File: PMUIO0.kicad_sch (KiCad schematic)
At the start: 3 parts, among them J1 Micro_SD_Card_Det1, U1 rv1126/rv1109

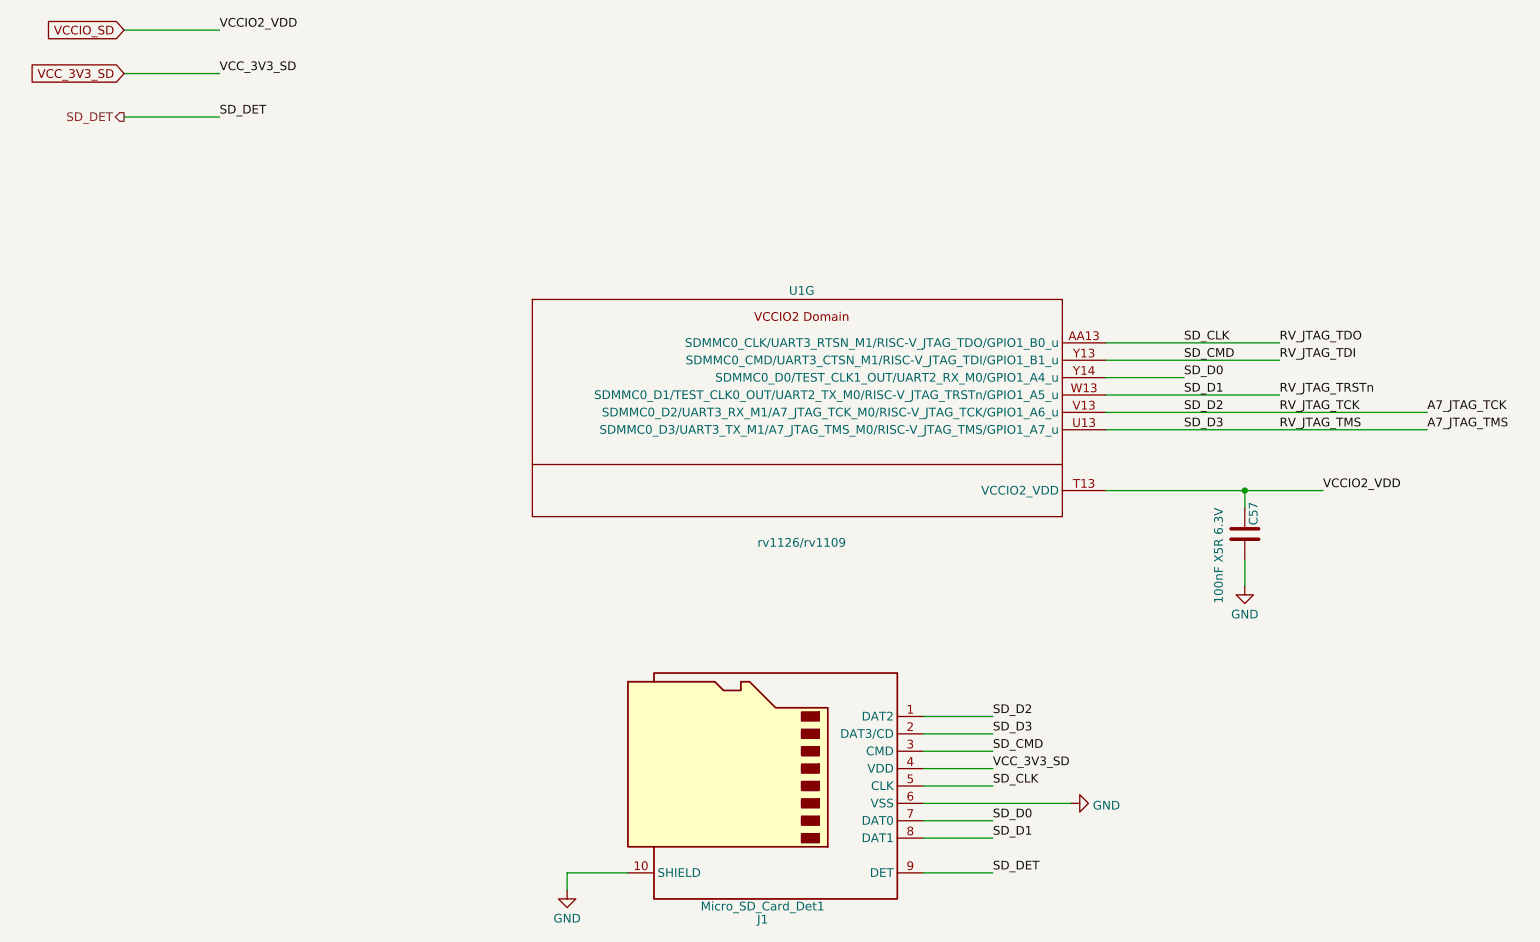
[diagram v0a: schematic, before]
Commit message: added MicroSD
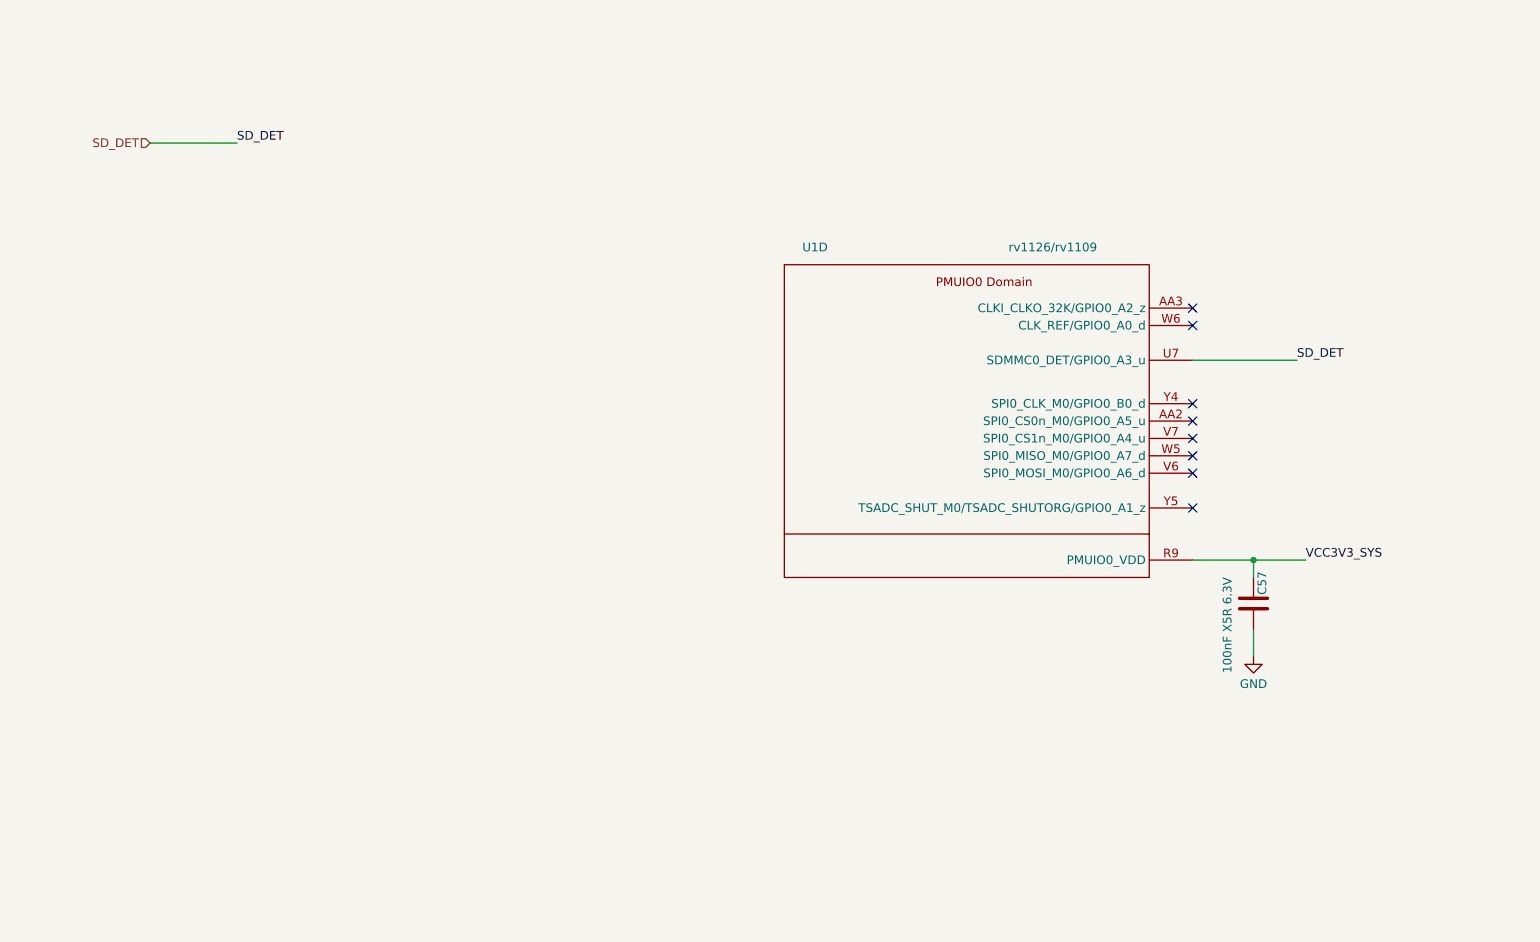
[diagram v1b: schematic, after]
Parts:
- removed J1: Micro_SD_Card_Det1, symbol Connector:Micro_SD_Card_Det1
- removed U1: rv1126/rv1109, symbol CPU_Rockchip:rv1126_rv1109
- added U1: rv1126/rv1109, symbol CPU_Rockchip:rv1126_rv1109
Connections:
- net SD_DET: now also U1.U7 (SDMMC0_DET/GPIO0_A3_u)
- net VCCIO_SD renamed VCC3V3_SYS
- net VCC3V3_SYS: now also U1.R9 (PMUIO0_VDD)
- no-connect marks 0 -> 8
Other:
- company: Qingdao IotPi Information Technology -> (none)
- title: Leaf RV1126 RK809 SDCard -> (none)

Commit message: updated footprints
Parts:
- U1: footprint (none) -> Rockchip_SoC:Rockchip_RV1126_FCCSP409LD_14.0x14.0mm
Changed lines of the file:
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@@
         )
         (path "/e3b58043-16a3-43c8-9fad-9c9784eebfa4/37e5f808-83b1-4839-b7a1-9684da8ab3e5"
-          (reference "#PWR076") (unit 1)
+          (reference "#PWR0127") (unit 1)
         )
       )
@@
       (effects (font (size 1.27 1.27)) (justify right))
     )
-    (property "Footprint" "" (at 180.34 104.14 0)
+    (property "Footprint" "Rockchip_SoC:Rockchip_RV1126_FCCSP409LD_14.0x14.0mm" (at 180.34 104.14 0)
       (effects (font (size 1.27 1.27)) hide)
     )
@@
         )
         (path "/e3b58043-16a3-43c8-9fad-9c9784eebfa4/37e5f808-83b1-4839-b7a1-9684da8ab3e5"
-          (reference "C101") (unit 1)
+          (reference "C139") (unit 1)
         )
       )

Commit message: updated Capacitors
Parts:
- C57: LCSC (none) -> C76934; Model (none) -> GRM033R61A104KE15D; Vendor (none) -> muRata(村田)
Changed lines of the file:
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@@
+      (effects (font (size 1.27 1.27)) hide)
+    )
+    (property "Description" "容值: 100nF 精度: ±10% 额定电压: 10V 材质(温度系数): X5R 材质:X5R" (at 195.58 105.41 0)
+      (effects (font (size 1.27 1.27)) hide)
+    )
+    (property "LCSC" "C76934" (at 195.58 105.41 0)
+      (effects (font (size 1.27 1.27)) hide)
+    )
+    (property "Model" "GRM033R61A104KE15D" (at 195.58 105.41 0)
+      (effects (font (size 1.27 1.27)) hide)
+    )
+    (property "Vendor" "muRata(村田)" (at 195.58 105.41 0)
       (effects (font (size 1.27 1.27)) hide)
     )

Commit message: layout SoC Power and DDR capacitors
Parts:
- C57: LCSC C76934 -> C76928; Model GRM033R61A104KE15D -> GRM033R60J104KE19D
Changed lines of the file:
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@@
       (effects (font (size 1.27 1.27)) hide)
     )
-    (property "Description" "容值: 100nF 精度: ±10% 额定电压: 10V 材质(温度系数): X5R 材质:X5R" (at 195.58 105.41 0)
+    (property "Description" "容值: 100nF 精度: ±10% 额定电压: 6.3V 材质(温度系数): X5R 材质:X5R" (at 195.58 105.41 0)
       (effects (font (size 1.27 1.27)) hide)
     )
-    (property "LCSC" "C76934" (at 195.58 105.41 0)
+    (property "LCSC" "C76928" (at 195.58 105.41 0)
       (effects (font (size 1.27 1.27)) hide)
     )
-    (property "Model" "GRM033R61A104KE15D" (at 195.58 105.41 0)
+    (property "Model" "GRM033R60J104KE19D" (at 195.58 105.41 0)
       (effects (font (size 1.27 1.27)) hide)
     )

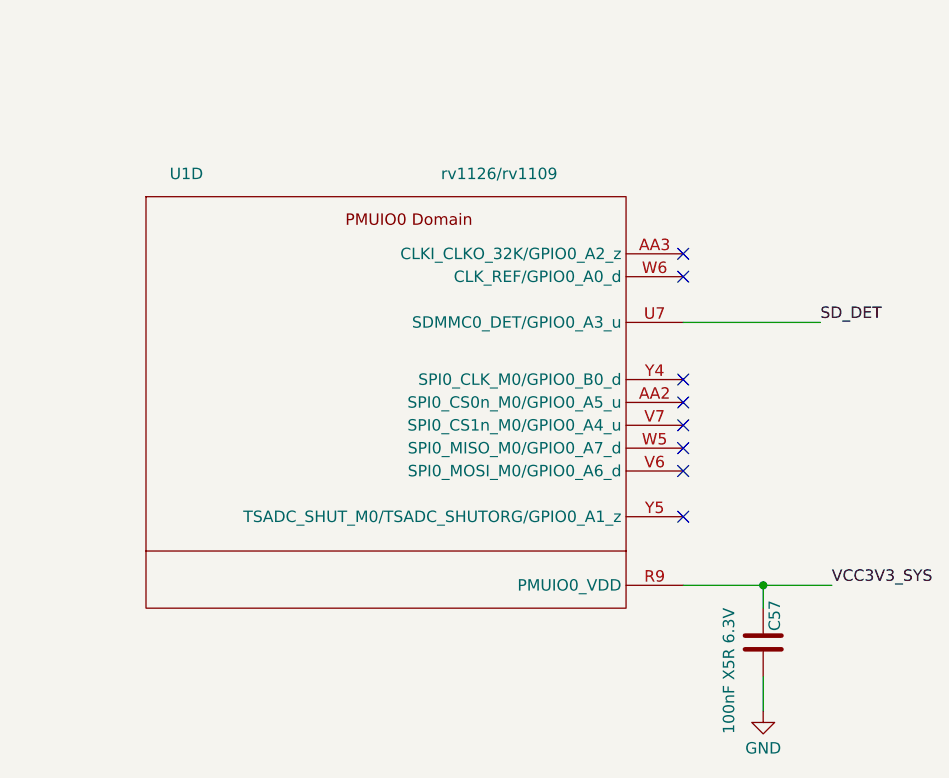
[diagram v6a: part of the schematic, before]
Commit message: fix some ERCs
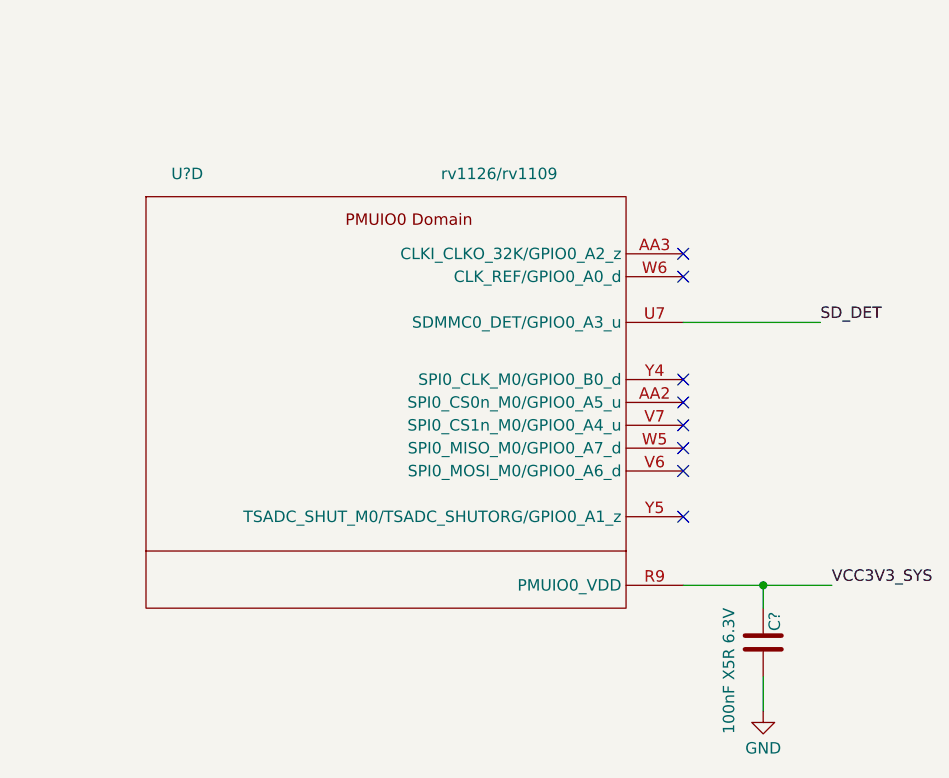
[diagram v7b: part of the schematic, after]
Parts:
- renumbered C57 to C?, U1 to U?
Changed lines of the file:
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@@
   (symbol (lib_id "power:GND") (at 195.58 113.03 0) (unit 1)
     (in_bom yes) (on_board yes) (dnp no) (fields_autoplaced)
-    (property "Reference" "#PWR074" (at 195.58 119.38 0)
+    (property "Reference" "#PWR?" (at 195.58 119.38 0)
       (effects (font (size 1.27 1.27)) hide)
     )
@@
       (project "leaf"
         (path "/e3b58043-16a3-43c8-9fad-9c9784eebfa4/4417415c-26f1-4372-988d-9fdf1c116b4b"
-          (reference "#PWR074") (unit 1)
+          (reference "#PWR?") (unit 1)
         )
         (path "/e3b58043-16a3-43c8-9fad-9c9784eebfa4/37e5f808-83b1-4839-b7a1-9684da8ab3e5"
-          (reference "#PWR0127") (unit 1)
+          (reference "#PWR0126") (unit 1)
         )
       )
@@
   (symbol (lib_id "CPU_Rockchip:rv1126_rv1109") (at 153.67 77.47 0) (unit 4)
     (in_bom yes) (on_board yes) (dnp no)
-    (property "Reference" "U1" (at 133.35 53.34 0)
+    (property "Reference" "U?" (at 133.35 53.34 0)
       (effects (font (size 1.27 1.27)) (justify right))
     )
@@
     (pin "Y21")
     (pin "C21")
-    (pin "D20")
     (pin "D21")
     (pin "E19")
@@
       (project "leaf"
         (path "/e3b58043-16a3-43c8-9fad-9c9784eebfa4/4417415c-26f1-4372-988d-9fdf1c116b4b"
-          (reference "U1") (unit 4)
+          (reference "U?") (unit 4)
         )
         (path "/e3b58043-16a3-43c8-9fad-9c9784eebfa4/37e5f808-83b1-4839-b7a1-9684da8ab3e5"
@@
   (symbol (lib_id "Device:C") (at 195.58 105.41 0) (unit 1)
     (in_bom yes) (on_board yes) (dnp no)
-    (property "Reference" "C57" (at 196.85 104.14 90)
+    (property "Reference" "C?" (at 196.85 104.14 90)
       (effects (font (size 1.27 1.27)) (justify left))
     )
@@
       (project "leaf"
         (path "/e3b58043-16a3-43c8-9fad-9c9784eebfa4/9453ad46-b3ff-4d4e-8aa6-7cc75aa0f522/f6658df5-193a-49b6-ab60-4ac3c0bbbc45"
-          (reference "C57") (unit 1)
+          (reference "C?") (unit 1)
         )
         (path "/e3b58043-16a3-43c8-9fad-9c9784eebfa4/9453ad46-b3ff-4d4e-8aa6-7cc75aa0f522/f6658df5-193a-49b6-ab60-4ac3c0bbbc45/b7d33089-b835-4c65-840f-b2075d1befa5"
-          (reference "C59") (unit 1)
+          (reference "C?") (unit 1)
         )
         (path "/e3b58043-16a3-43c8-9fad-9c9784eebfa4/9453ad46-b3ff-4d4e-8aa6-7cc75aa0f522"
-          (reference "C84") (unit 1)
+          (reference "C?") (unit 1)
         )
         (path "/e3b58043-16a3-43c8-9fad-9c9784eebfa4/cc9fb3ac-19c3-47a8-ba7d-678b4d514ff0/8aa2eca1-edfe-4e9d-a854-96f51e82fbdb"
-          (reference "C90") (unit 1)
+          (reference "C?") (unit 1)
         )
         (path "/e3b58043-16a3-43c8-9fad-9c9784eebfa4/4417415c-26f1-4372-988d-9fdf1c116b4b"
-          (reference "C100") (unit 1)
+          (reference "C?") (unit 1)
         )
         (path "/e3b58043-16a3-43c8-9fad-9c9784eebfa4/37e5f808-83b1-4839-b7a1-9684da8ab3e5"
-          (reference "C139") (unit 1)
+          (reference "C135") (unit 1)
         )
       )

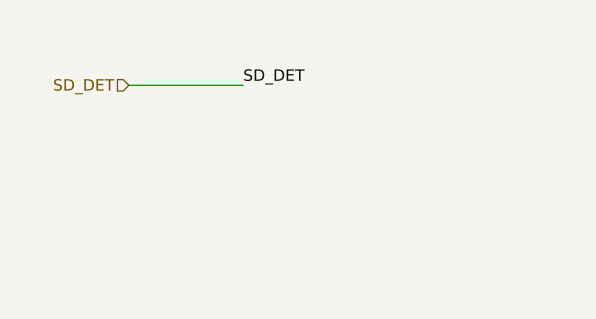
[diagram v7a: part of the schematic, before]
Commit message: fix ERC
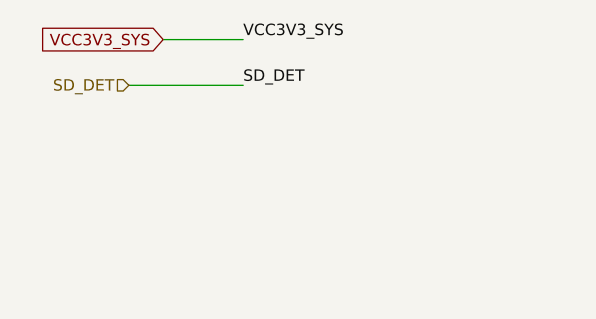
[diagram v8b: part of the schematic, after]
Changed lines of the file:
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@@
+    (stroke (width 0) (type default))
+  )
+  (wire (pts (xy 38.1 33.02) (xy 46.99 33.02))
     (stroke (width 0) (type default))
   )
@@
     (effects (font (size 1.27 1.27)) (justify left bottom))
   )
+  (label "VCC3V3_SYS" (at 46.99 33.02 0) (fields_autoplaced)
+    (effects (font (size 1.27 1.27)) (justify left bottom))
+  )
+  (global_label "VCC3V3_SYS" (shape input) (at 38.1 33.02 180) (fields_autoplaced)
+    (effects (font (size 1.27 1.27)) (justify right))
+    (property "Intersheetrefs" "${INTERSHEET_REFS}" (at 23.5828 33.02 0)
+      (effects (font (size 1.27 1.27)) (justify right) hide)
+    )
+  )
   (hierarchical_label "SD_DET" (shape input) (at 34.29 38.1 180) (fields_autoplaced)
